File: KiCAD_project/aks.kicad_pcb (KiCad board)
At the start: 2 copper layers, 30 x 35 mm, 40 parts, among them M3 ОтверстиеD3

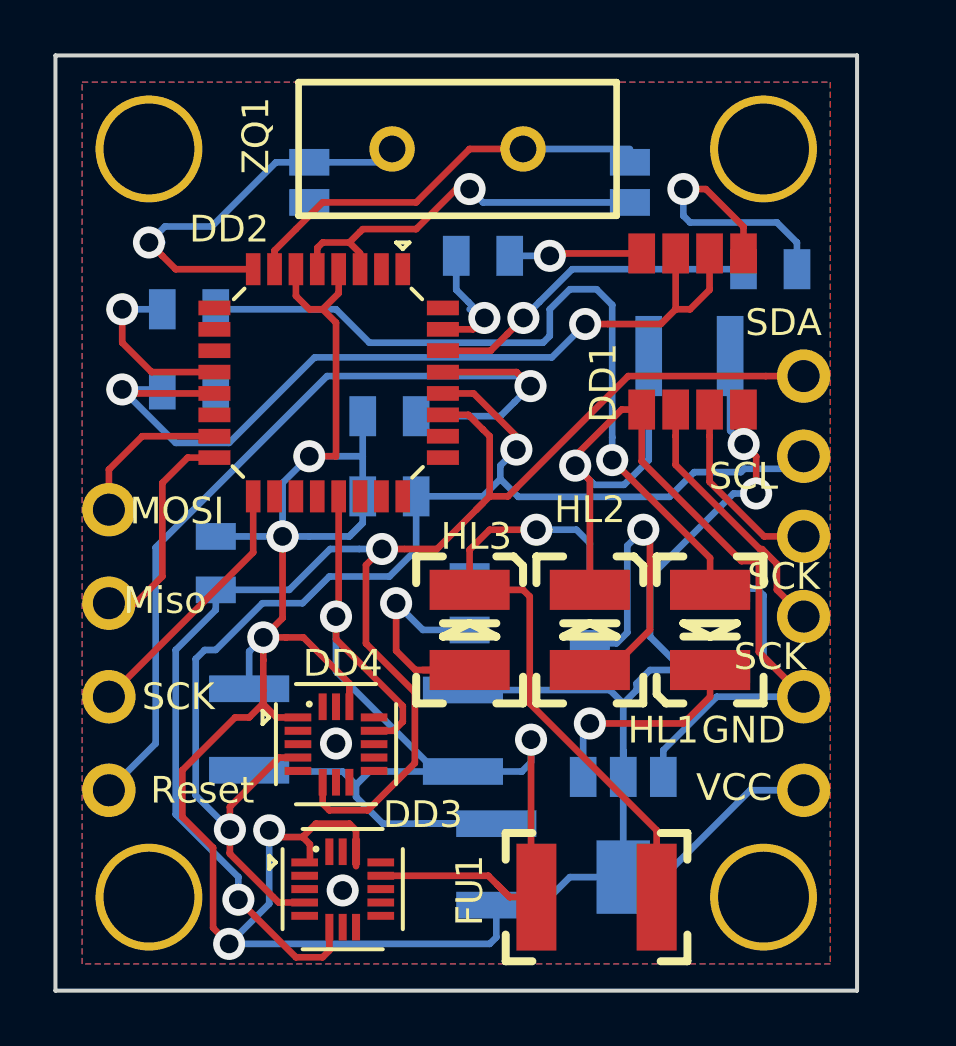
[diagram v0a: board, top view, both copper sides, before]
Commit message: подготовлены GERBER файлы, exel-заказа не заполнена
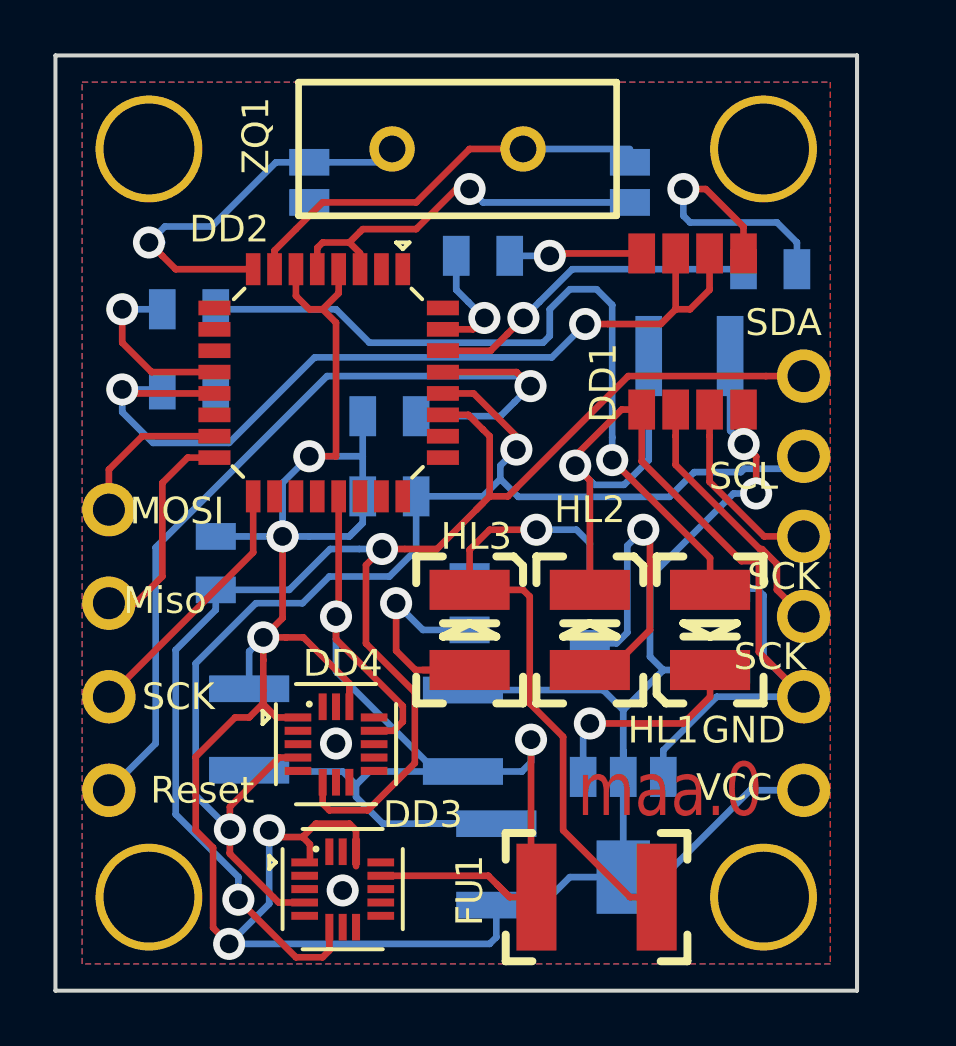
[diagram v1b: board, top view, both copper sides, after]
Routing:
- net Ucc: track 124.8 -> 122.9 mm
- net GND: track 120.5 -> 119.8 mm
- net GND1: track 26.1 -> 26.7 mm
- net TX: track 4.99 -> 4.49 mm
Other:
- board text added: "maa.0"

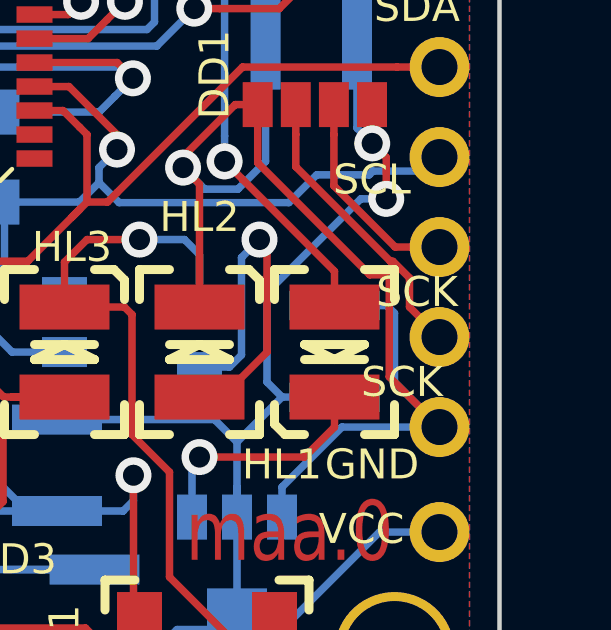
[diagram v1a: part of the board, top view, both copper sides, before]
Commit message: отлажен UART(RS485), I2C не работает
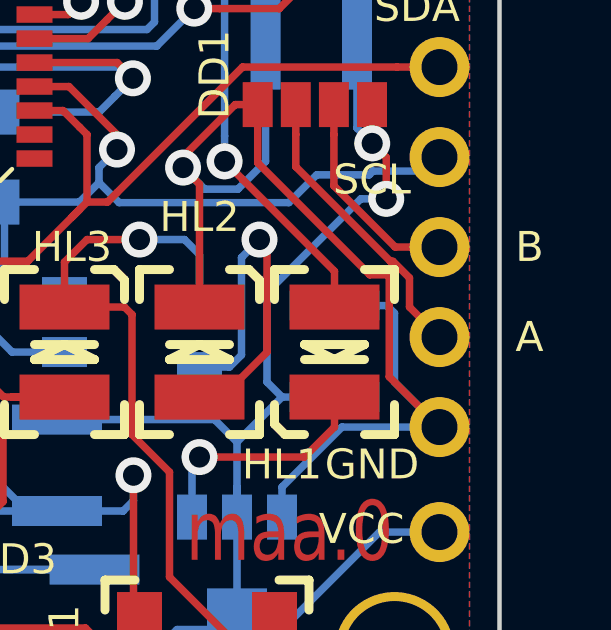
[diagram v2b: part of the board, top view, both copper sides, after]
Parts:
- XS6: value SCK -> A
- XS7: value SCK -> B
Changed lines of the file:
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@@
       (effects (font (size 1 1) (thickness 0.15)))
     )
-    (fp_text value SCK (at -1.25 1.5) (layer F.SilkS)
+    (fp_text value A (at 3 0) (layer F.SilkS)
       (effects (font (size 1 1) (thickness 0.15)))
     )
@@
       (effects (font (size 1 1) (thickness 0.15)))
     )
-    (fp_text value SCK (at -0.75 1.5) (layer F.SilkS)
+    (fp_text value B (at 3 0) (layer F.SilkS)
       (effects (font (size 1 1) (thickness 0.15)))
     )
